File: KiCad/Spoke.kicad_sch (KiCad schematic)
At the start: 122 parts, among them J1 BAT+, J2 BAT-, J26 CHG-, J27 CHG+, J3 BL-A, J4 BL-C, J5 PLS-1x6, J6 PLS-1x3, J7 GCT USB4105/USB4110, J8 B2B-PH-K-S, J9 Amphenol 132289, Q1 AO3407A, Q5 AO3400, Q6 AO3400, Q7 AO3400, SW10 ESC/DN, SW5 OK/UP, SW6 ESC/DN, SW7 PWR, SW8 BOOT, SW9 OK/UP, U1 LM3671MF-3.3, U10 LSM303DLHC, U2 74HC4052PW, U3 STM32F103C8T6, U4 CP2102N-A02-GQFN28, U9 TP4056, X1 8MHz

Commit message: Add SP0503BAHTG
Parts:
- added U5: SP0503BAHTG, symbol Spoke:SP0503BAHTG
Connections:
- net GND: now also U5.1 (A)
- net VBUS: now also U5.4 (K)
- net at J7.A6 (D+), J7.B6 (D+), U4.4 (D+): now also U5.3 (K)
- net at J7.A7 (D-), J7.B7 (D-), U4.5 (D-): now also U5.2 (K)
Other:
- moved on the sheet: C11, C12, C13, C14, C15, C16, C17, C18, C19, C20, C21, C22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

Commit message: Add URX pull-ups
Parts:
- added R37, R38, R39: 100kR, Spoke:R0805, symbol Spoke:R
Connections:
- net 3V3: now also R37.1, R38.2
- net BLE_RXD: now also R37.2
- net CONSOLE_RXD: now also R38.1
- net USB_RXD: now also R39.1
- net VUSB3V3: now also R39.2
- no-connect marks 30 -> 34
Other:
- moved on the sheet: C29, C30, C5, D7, J26, J27, J6, R31, R34, R8, TP12, TP13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

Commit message: SCH finished, annotate all
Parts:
- renumbered A2 to A1, A4 to A2, A1 to A3, A5 to A4, C29 to C1, C11 to C10, C9 to C11, C24 to C12, C7 to C13, C13 to C14, C1 to C15, C2 to C16, C3 to C17, C14 to C18, C4 to C19, C10 to C2, C25 to C20, C15 to C24, C16 to C25, C32 to C26, C31 to C27, C5 to C28, C12 to C29, C17 to C3, C27 to C30, C26 to C31, C28 to C32, C18 to C4, C30 to C5, C19 to C6, C6 to C7, C20 to C8, C8 to C9, D7 to D2, D5 to D3, D6 to D4, J8 to J1, J4 to J10, J9 to J11, J1 to J2, J2 to J3, J7 to J4, J27 to J5, J26 to J6, J5 to J7, J6 to J8, J3 to J9, L2 to L1, LS2 to LS1, Q5 to Q2, Q7 to Q3, Q6 to Q4, R19 to R1, R39 to R10, R8 to R11, R5 to R12, R21 to R13, R23 to R14, R26 to R15, R4 to R16, R38 to R17, R1 to R18, R36 to R19, R3 to R2, R30 to R20, R33 to R21, R24 to R22, R25 to R23, R35 to R24, R9 to R25, R12 to R26, R37 to R27, R17 to R28, R22 to R29, R20 to R3, R15 to R30, R16 to R31, R29 to R32, R32 to R33, R11 to R34, R14 to R35, R6 to R36, R2 to R37, R27 to R38, R28 to R39, R34 to R4, R10 to R5, R13 to R6, R18 to R8, R31 to R9, SW7 to SW1, SW5 to SW2, SW6 to SW3, SW9 to SW4, SW10 to SW5, SW8 to SW6, TP21 to TP1, TP20 to TP10, TP23 to TP11, TP8 to TP12, TP24 to TP13, TP9 to TP14, TP25 to TP15, TP10 to TP16, TP12 to TP2, TP13 to TP3, TP14 to TP4, TP15 to TP5, TP16 to TP6, TP18 to TP7, TP17 to TP8, TP19 to TP9, U5 to U1, U9 to U2, U4 to U3, U1 to U4, U2 to U5, U3 to U6, U10 to U7

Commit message: Annotate SCH
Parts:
- R13, R15, R19: value 10kR -> 100kR
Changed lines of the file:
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@@
 		(dnp no)
 		(property "Reference" "J3"
-			(at 46.99 68.58 90)
+			(at 45.72 68.58 90)
 			(effects
 				(font
@@
 		)
 		(property "Value" "BAT-"
-			(at 49.53 71.12 90)
+			(at 48.26 71.12 90)
 			(effects
 				(font
@@
 			)
 		)
-		(property "Value" "10kR"
+		(property "Value" "100kR"
 			(at 212.09 364.49 0)
 			(effects
@@
 			)
 		)
-		(property "Value" "10kR"
+		(property "Value" "100kR"
 			(at 234.95 233.6799 90)
 			(effects
@@
 			)
 		)
-		(property "Value" "10kR"
+		(property "Value" "100kR"
 			(at 205.74 326.3899 90)
 			(effects

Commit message: ERC done
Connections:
- net 3V3 renamed +3V3
- net VBAT renamed +BATT
- net VUSB3V3 renamed VDD

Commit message: Assign footprint
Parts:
- A1: footprint (none) -> Spoke:E104-BT5005A
- A2: footprint (none) -> Spoke:E22
- A4: footprint (none) -> Spoke:GN-801
- C1, C30, C5: footprint Spoke:C0805 -> Spoke:C1206
- C10, C11, C12, C14, C15, C16, C17, C18, C19, C2, C20, C21, C22, C25, C28, C29, C31, C32, C4, C6, C9: footprint Spoke:C0805 -> Spoke:C0603
- D2, D3, D4: footprint (none) -> Spoke:LED1206
- J1: footprint (none) -> Spoke:B2B-PH-2.0
- J11: footprint (none) -> Spoke:SMA
- J4: footprint (none) -> Spoke:USB_C_16p_GCT4105
- L1: footprint (none) -> Spoke:L1616
- LS1: footprint (none) -> Spoke:Buzzer
- Q1, Q2, Q3, Q4: footprint (none) -> Spoke:SOT-23
- R1, R10, R11, R12, R13, R14, R15, R16, R17, R18, R19, R2, R20, R21, R22, R23, R24, R25, R26, R27, R28, R29, R3, R30, R31, R32, R33, R34, R35, R36, R38, R39, R4, R5, R6, R7, R8, R9: footprint Spoke:R0805 -> Spoke:R0603
- R37: footprint Spoke:R0805 -> Spoke:R1206
- SW1, SW2, SW3, SW4, SW5, SW6: footprint (none) -> Spoke:Button_6x6
- U1: footprint (none) -> Spoke:SOT-143
- U3: footprint (none) -> Spoke:QFN-28
- U4: footprint (none) -> Spoke:SOT-23-5
- U5: footprint (none) -> Spoke:TSSOP-16
- X1: footprint (none) -> Spoke:Xtal_3225

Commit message: Simplify UART lines, add USB UART conn
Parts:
- removed R14: 1kR, Spoke:R0603, symbol Spoke:R
- added J7: PLS-1x3, Spoke:Header_1x3, symbol Spoke:PLS-1x3
- renumbered J9 to J10, J10 to J11, J11 to J12, J7 to J8, J8 to J9, R23 to R11, R15 to R14, R16 to R15, R18 to R16, R19 to R17, R20 to R18, R21 to R19, R24 to R20, R11 to R21, R17 to R22, R22 to R23, R25 to R24, R26 to R25, R27 to R26, R28 to R27, R29 to R28, R30 to R29, R31 to R30, R32 to R31, R33 to R32, R34 to R33, R35 to R34, R36 to R35, R37 to R36, R38 to R37, R39 to R38
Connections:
- net BLE_TXD: now also R23.1, U5.1 (2Y0); no longer A1.12 (TXD), R23.2
- net CONSOLE_TXD: now also J9.1, U5.13 (1Z); no longer U6.30 (PA9)
- net GND: now also J7.3
- net USB_RXD: now also J7.2
- net USB_TXD: now also U5.5 (2Y1), J7.1; no longer U3.26 (TXD)
- net at R11.1: now also U3.26 (TXD); no longer U5.5 (2Y1)
- net at R21.2: now also U6.30 (PA9); no longer J9.1
- new net: A1.12 (TXD), R23.2
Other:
- moved on the sheet: J9, R10, R11, R18, R19, R21, R22, R23, TP2, TP3

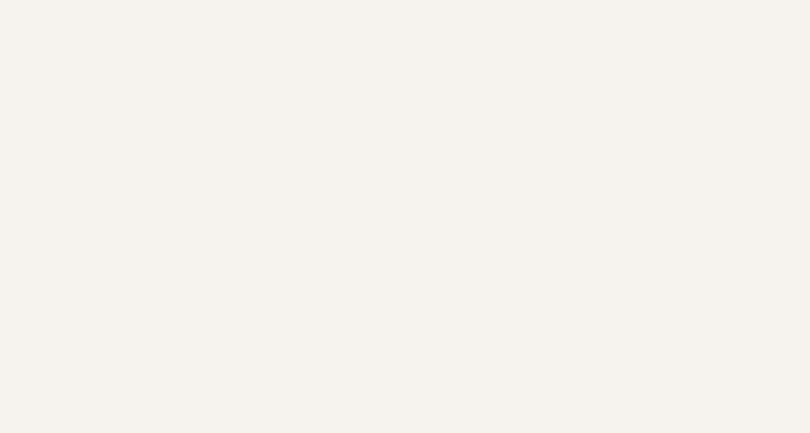
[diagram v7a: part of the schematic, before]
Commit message: Add MHs and import to PCB
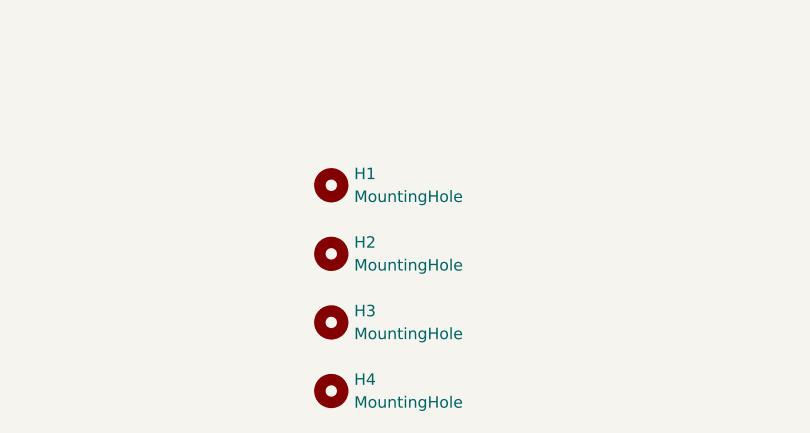
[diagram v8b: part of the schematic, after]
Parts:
- added H1, H2, H3, H4: MountingHole, MountingHole:MountingHole_3.2mm_M3, symbol Mechanical:MountingHole
